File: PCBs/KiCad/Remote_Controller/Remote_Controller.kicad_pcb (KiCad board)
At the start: 4 copper layers, 160 x 78.8 mm, 81 parts, among them J201 USB_C_Receptacle_USB2.0_16P, Q101 IRF7319, Q102 IRFML8244TRPBF, Q103 IRFML8244TRPBF, Q201 SS8050-G, Q202 SS8050-G, SW101 Power Switch, SW201 SW_Push, SW301 SW_Push, SW302 SW_Push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

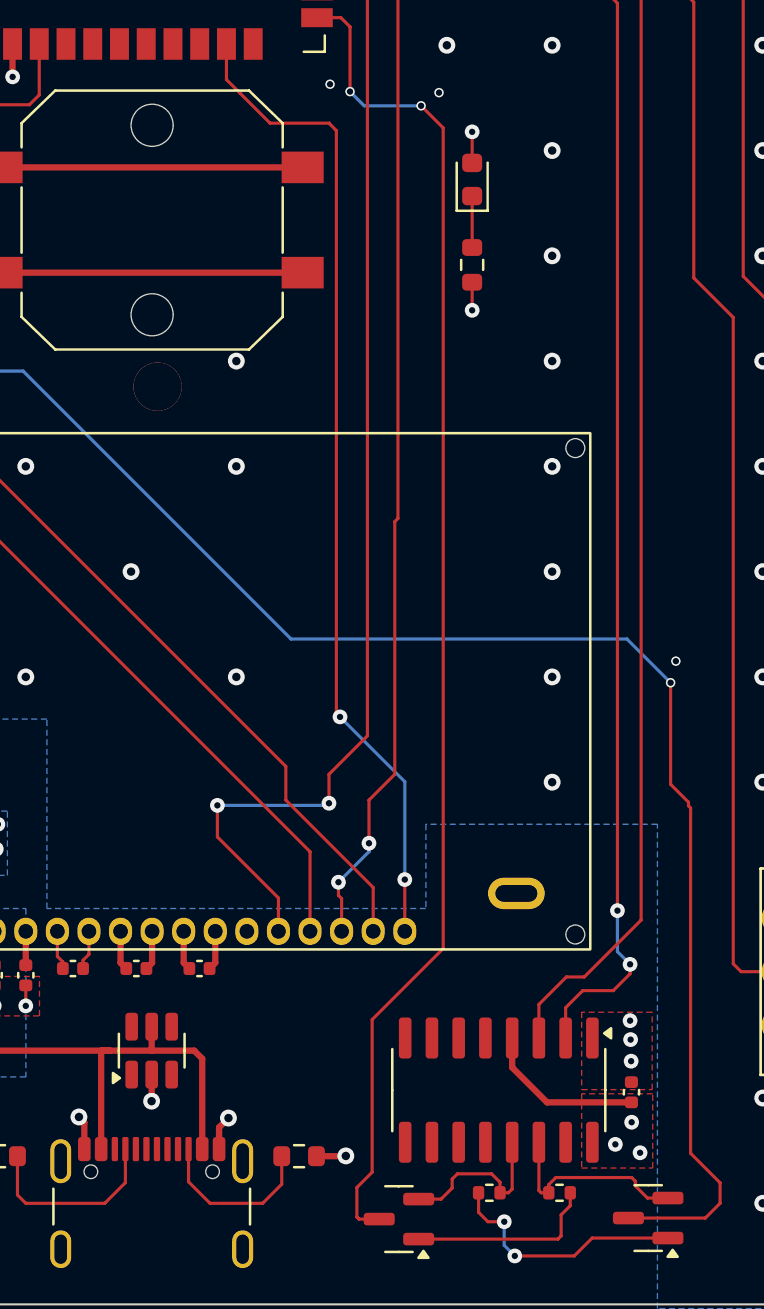
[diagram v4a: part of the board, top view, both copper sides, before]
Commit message: Added differential USB signal
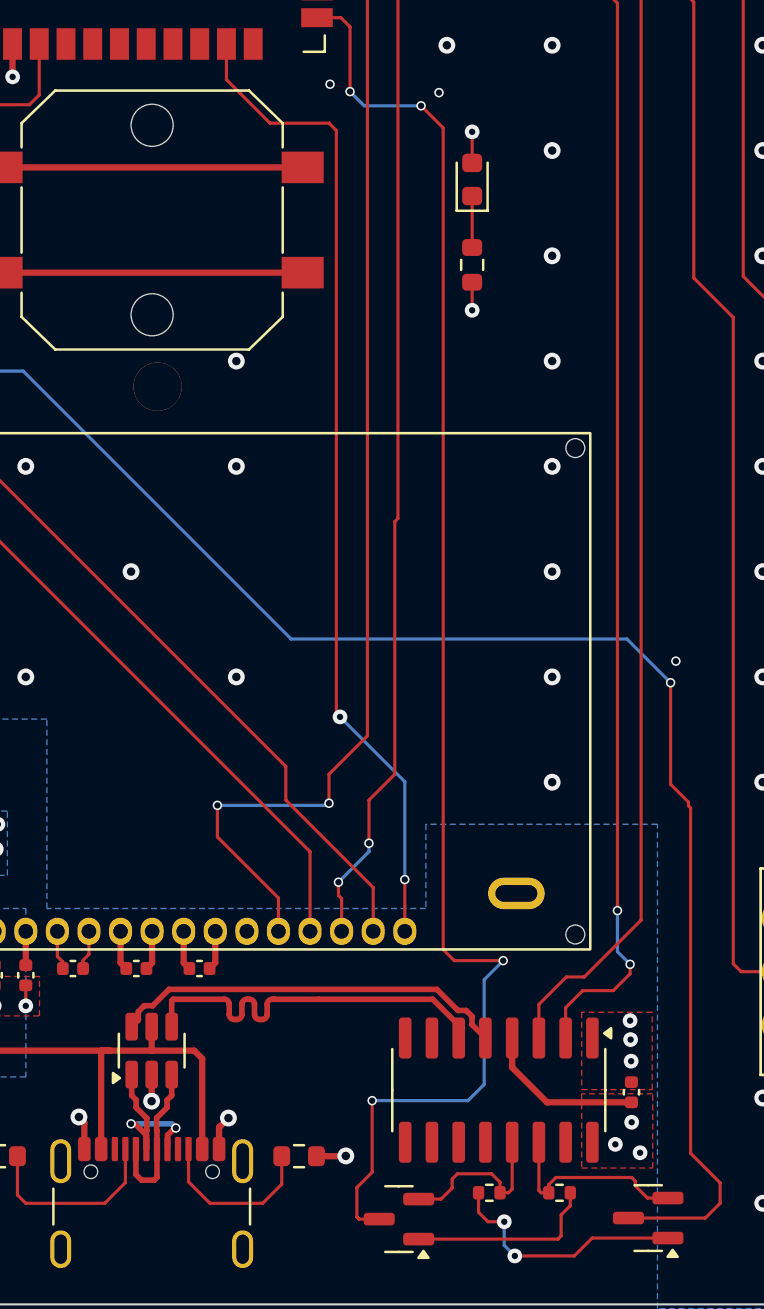
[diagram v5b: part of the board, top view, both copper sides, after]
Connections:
- U201 pad 1: /[2] Microcontroller And Bluetooth/D_RAW- -> /[2] Microcontroller And Bluetooth/D_RAW+
- U201 pad 3: /[2] Microcontroller And Bluetooth/D_RAW+ -> /[2] Microcontroller And Bluetooth/D_RAW-
- U201 pad 4: /[2] Microcontroller And Bluetooth/D+ -> /[2] Microcontroller And Bluetooth/D-
- U201 pad 6: /[2] Microcontroller And Bluetooth/D- -> /[2] Microcontroller And Bluetooth/D+
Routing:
- net /[2] Microcontroller And Bluetooth/D+: track 0.00 -> 19.0 mm
- net /[2] Microcontroller And Bluetooth/D-: track 0.00 -> 19.0 mm
- net /[2] Microcontroller And Bluetooth/D_RAW+: track 0.00 -> 8.85 mm, vias 0 -> 2
- net /[2] Microcontroller And Bluetooth/D_RAW-: track 0.00 -> 7.56 mm
- net /[2] Microcontroller And Bluetooth/IO0: track 64.5 -> 70.9 mm, vias 2 -> 4

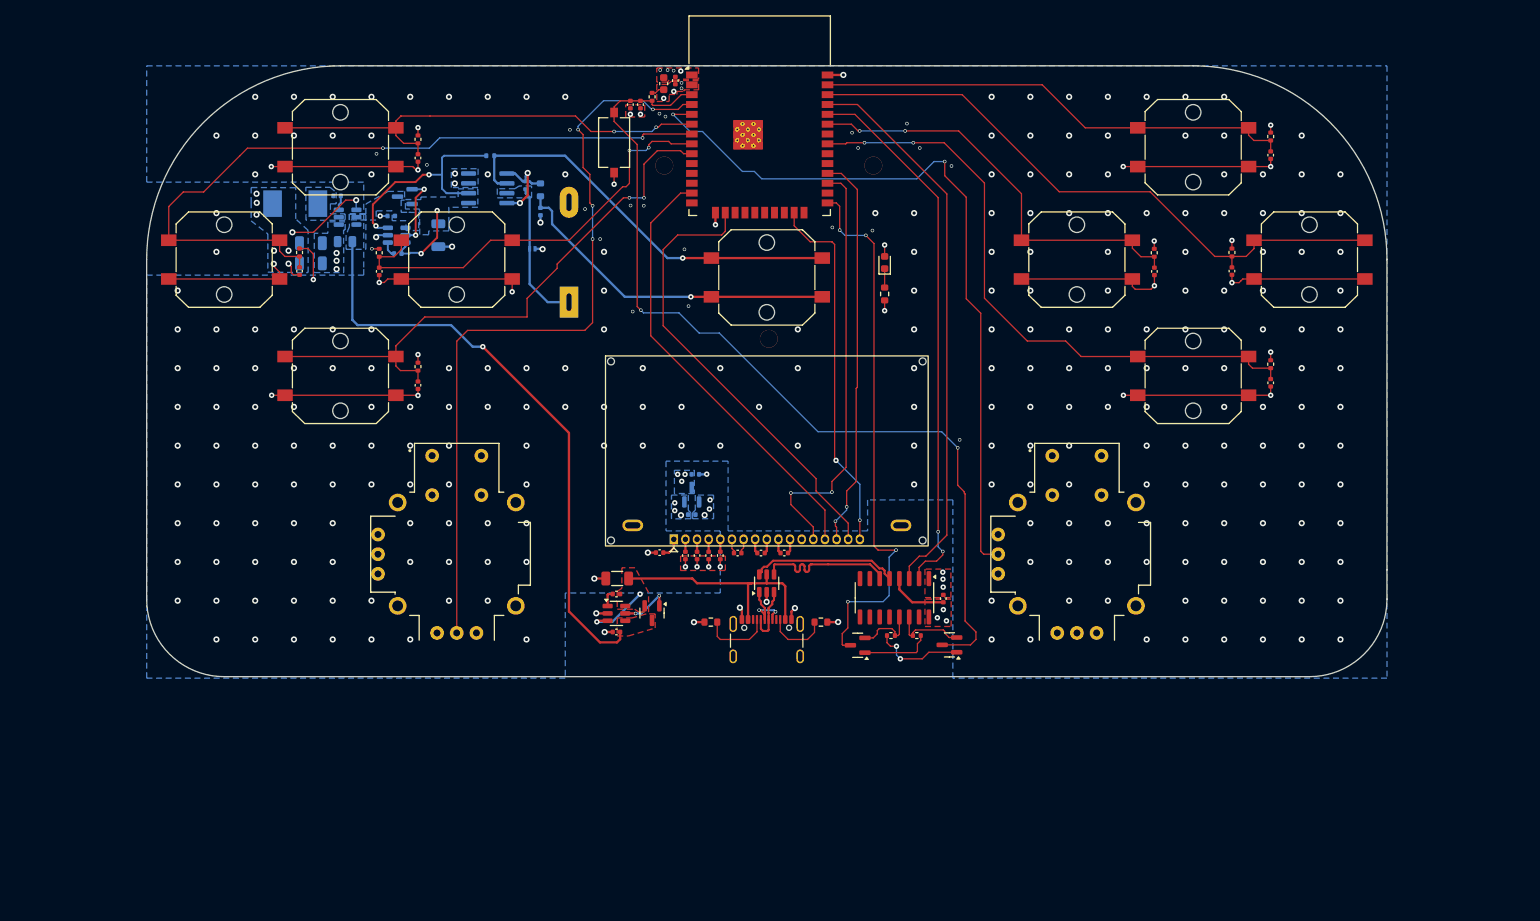
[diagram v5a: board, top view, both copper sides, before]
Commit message: Added silkscreen text and made manufacturing files
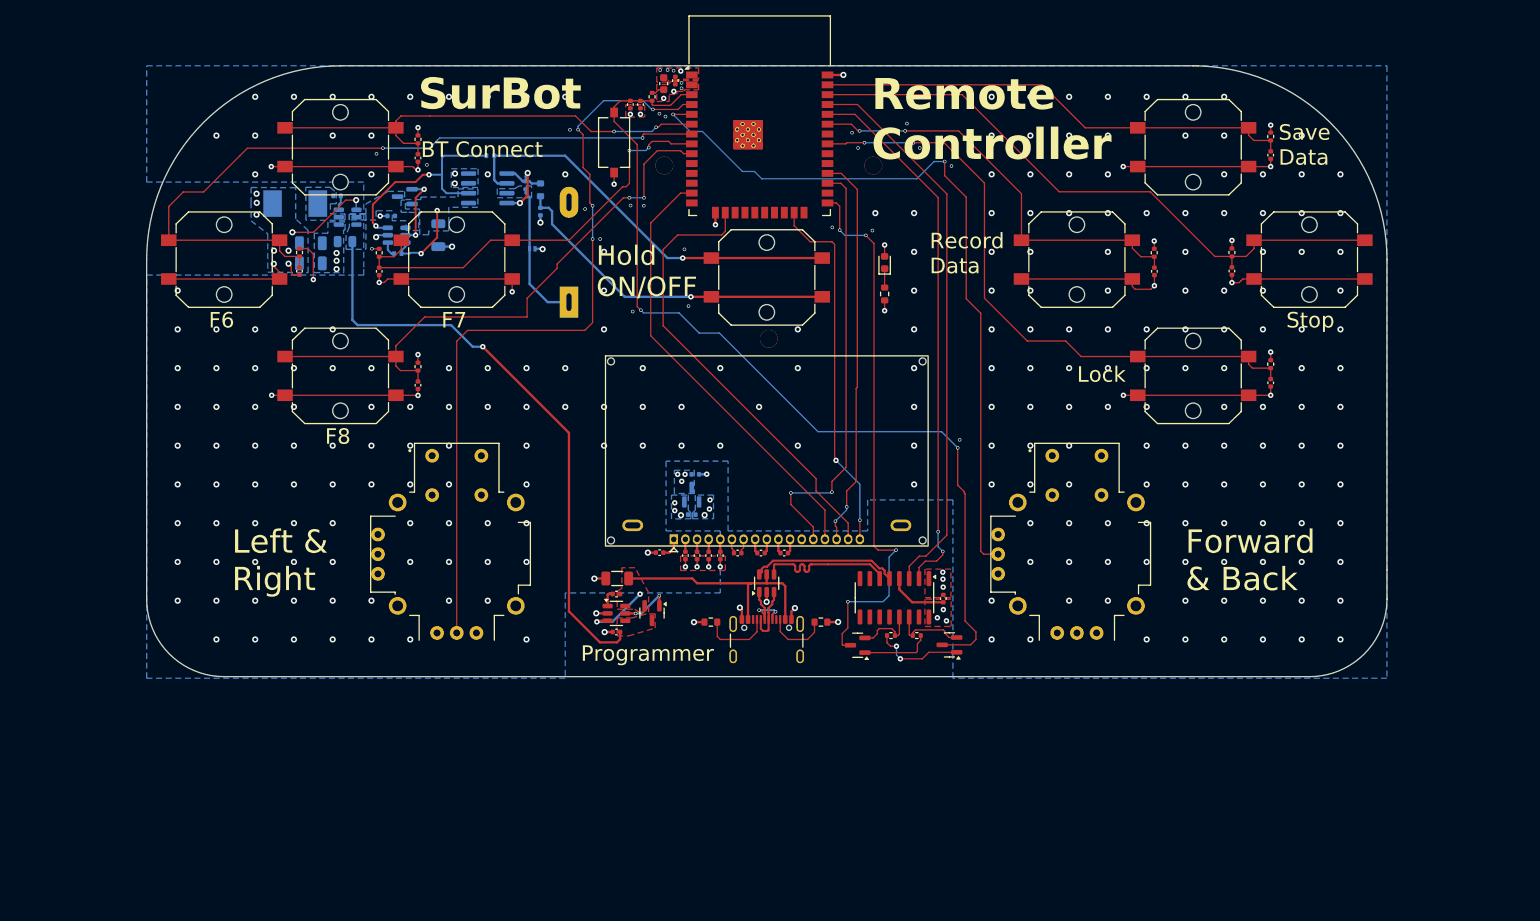
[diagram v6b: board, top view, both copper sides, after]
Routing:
- net GND: vias 317 -> 313
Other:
- board text added: "BT Connect"
- board text added: "F6"
- board text added: "F7"
- board text added: "F8"
- board text added: "Forward & Back"
- board text added: "Hold ON/OFF"
- board text added: "Left & Right"
- board text added: "Lock"
- board text added: "Programmer"
- board text added: "Record Data"
- board text added: "Remote Controller"
- board text added: "Save Data"
- board text added: "Stop"
- board text added: "SurBot"

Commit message: Added mounting holes
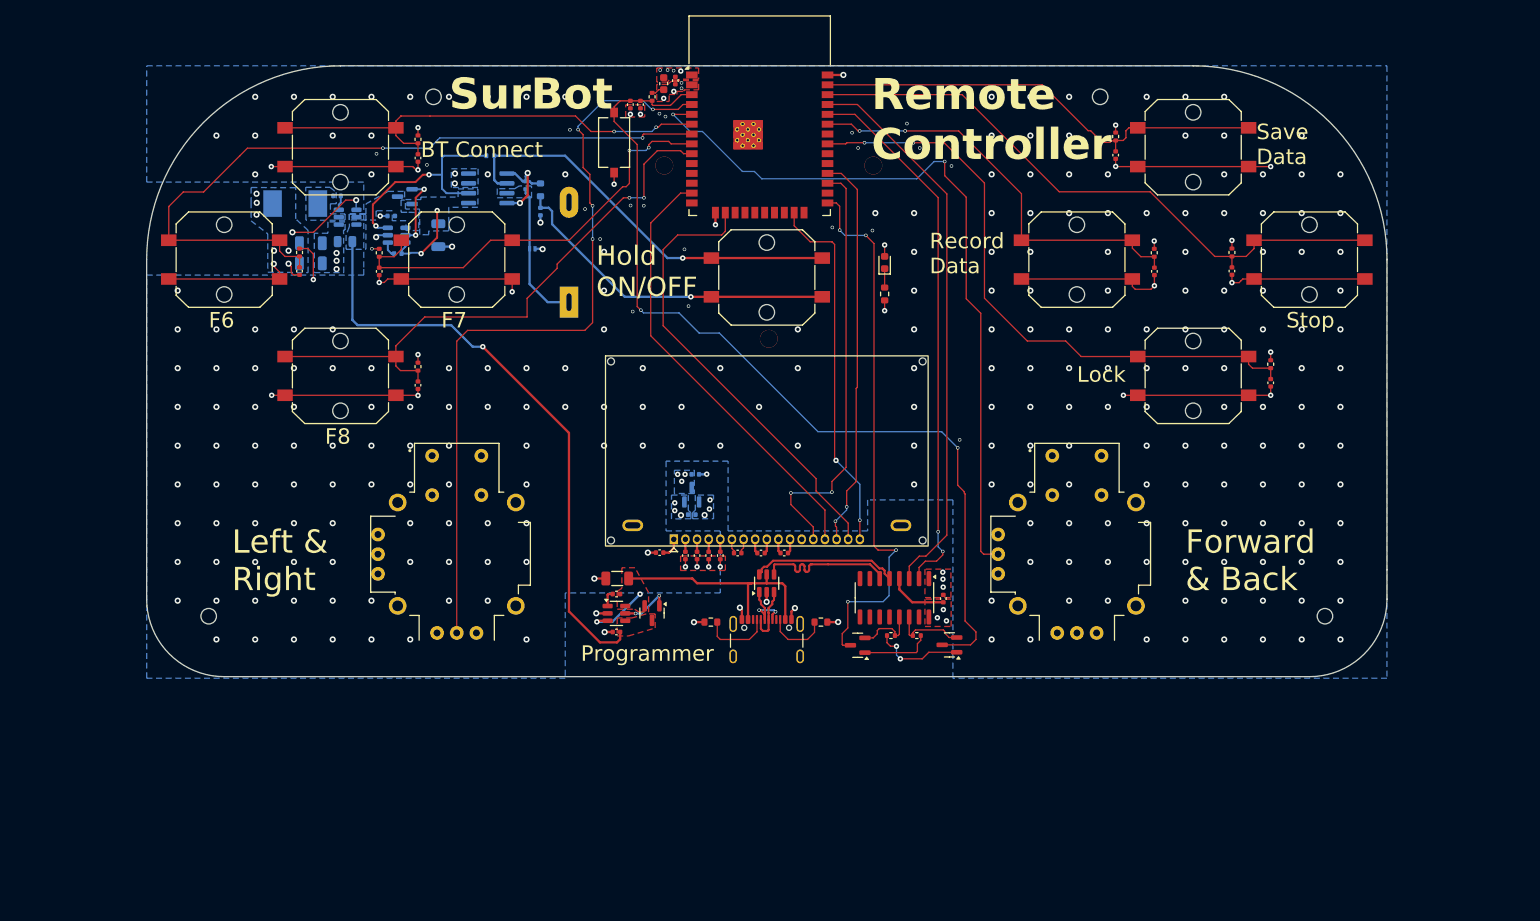
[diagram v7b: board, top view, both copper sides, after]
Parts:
- added H1: MountingHole, MountingHole:MountingHole_2mm, F.Cu at (184.0, 50.0)
- added H2: MountingHole, MountingHole:MountingHole_2mm, F.Cu at (98.0, 50.0)
- added H3: MountingHole, MountingHole:MountingHole_2mm, F.Cu at (69.0, 117.0)
- added H4: MountingHole, MountingHole:MountingHole_2mm, F.Cu at (213.0, 117.0)
- moved C309 20.0 mm to (186.0, 57.5)
- moved R301 20.0 mm to (186.0, 55.1)
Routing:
- net SAVE_DATA: track 62.1 -> 60.1 mm
- net +3V3: track 179.3 -> 180.3 mm
- net GND: vias 313 -> 311
